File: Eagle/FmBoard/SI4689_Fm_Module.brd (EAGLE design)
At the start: 32.5 x 42.7 mm, 69 parts, among them IC1 TPS79318DBVR, IC2 SI4688-A10-GM, U1 TXS0104EPWR, U2 3.3V/150mA, X2 19.2MHz

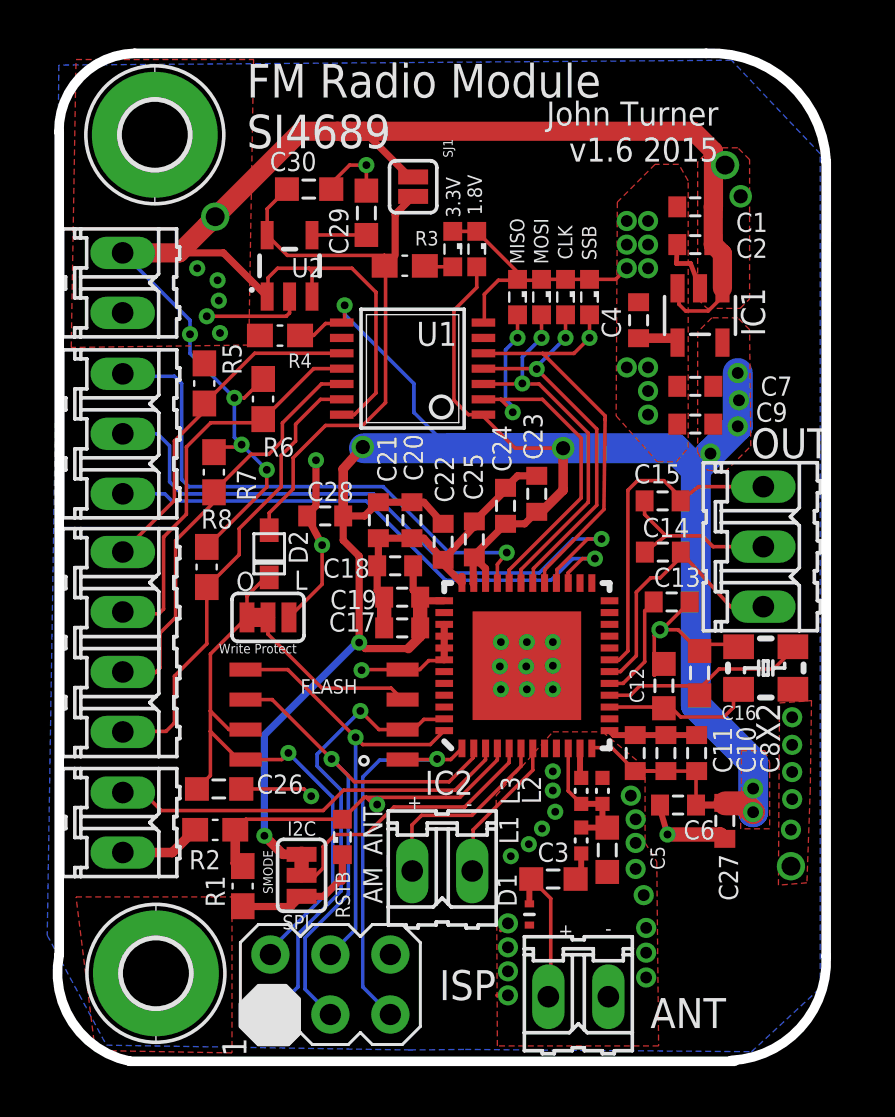
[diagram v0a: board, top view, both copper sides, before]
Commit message: Updated to the now working v1.7 of the radio module Made Radio Module arudino compatible so that it can be plugged directly into the arudino Moved to a S25FL132K0XMFI041 flash chip due to being cheaper and easier to program.
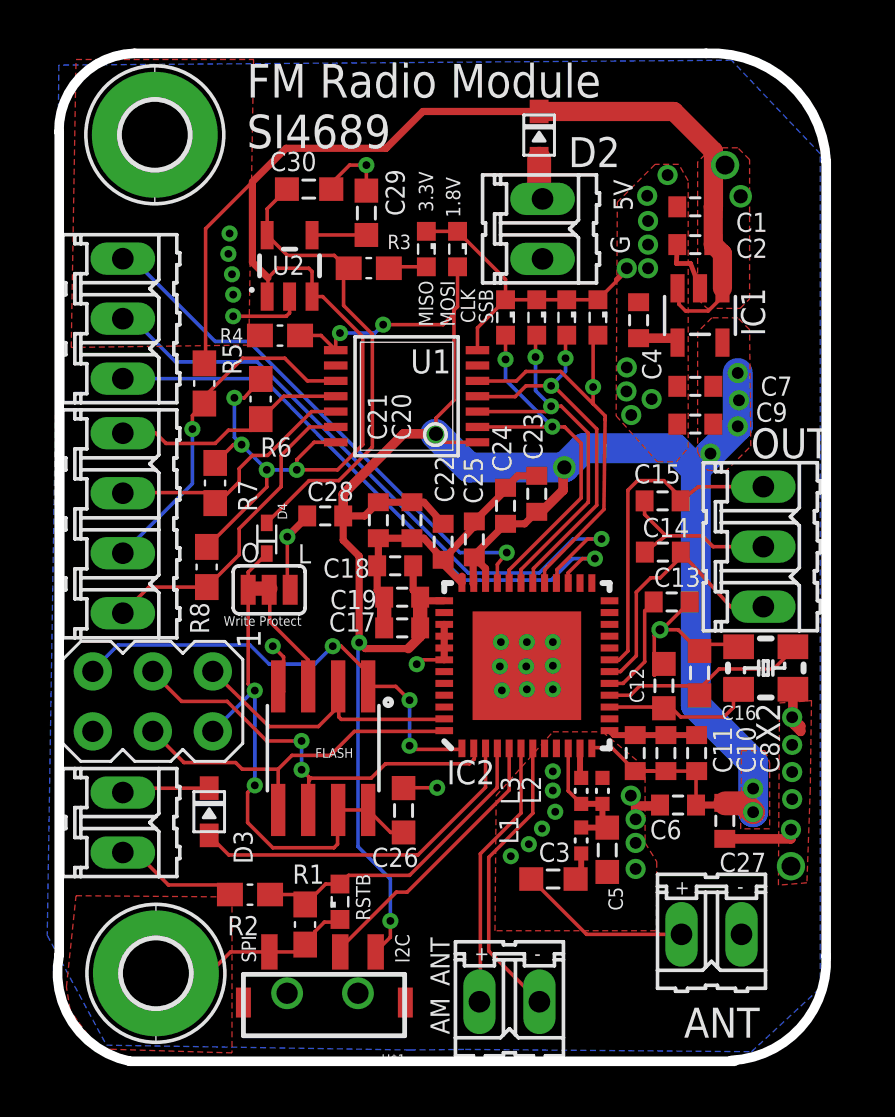
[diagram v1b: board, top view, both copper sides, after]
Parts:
- removed D1: ESD9L5.0, generisch:SOD923
- removed ISP: AVRISP-6, adafruit:AVRISP
- removed SJ1: SOLDERJUMPERNC, SparkFun-Retired:SJ_2S
- removed SMODE: (no value), SparkFun-Retired:SJ_3
- added D3: (no value), adafruit:SOD-323F
- added D4: (no value), SparkFun-DiscreteSemi:SOD523
- added ISP1: AVRISP-6, adafruit:AVRISP
- added U$1: SWITCH_SPDTMOUSER, SparkFun-Electromechanical:SSSS810701
- FLASH: value SST25VF016BSOIC -> SPI_FLASH-X25XXSMD; device john:SOIC8 -> SparkFun-DigitalIC:SO08
- IC2: value SI4688-A10-GM -> SI4689GM; device SI4688-A10-GM:QFN48 -> john:QFN48
- moved D2 21.1 mm to (20.6, 38.6), turned to 90 degrees
- moved POWER 17.9 mm to (20.5, 34.6)
- moved C26 7.88 mm to (14.9, 9.96), turned to 90 degrees
- moved ANT 6.23 mm to (27.9, 4.97)
- moved AM_ANT 6.23 mm to (19.4, 2.11)
- moved CONTROL 5.03 mm to (2.74, 22.1)
- moved DIGITALAUDIO 4.88 mm to (2.74, 30.8)
- moved R2 3.11 mm to (8.38, 6.40)
- moved R1 3.10 mm to (10.7, 5.13)
- moved RSTB 2.75 mm to (12.2, 6.10)
- moved FLASH 1.61 mm to (11.5, 12.6), turned to 180 degrees
- moved R3 1.53 mm to (13.4, 32.9)
- moved U1 1.20 mm to (15.0, 27.5)
- moved WP 1.17 mm to (9.19, 19.3)
- moved 3.3V 1.12 mm to (15.8, 33.7)
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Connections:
- removed net SPI0_CE0_N: CONTROL.1, R5.1, U1.10
- new net N$10: CHIP.1, D3.C
- new net N$19: D2.A, POWER.1
- new net SPI0_SSB: CONTROL.3, R5.1, U1.10
- net +1V8: now also U$1.S; no longer SMODE.3
- net 3.3V: now also D4.A; no longer D2.A, SJ1.2
- net FLASH_CE: now also ISP1.5; no longer ISP.5
- net FLASH_SCK: now also ISP1.3; no longer ISP.3
- net FLASH_SI: now also ISP1.4; no longer ISP.4
- net FLASH_SO: now also ISP1.1; no longer ISP.1
- net FLASH_VIN: now also D4.C, ISP1.2; no longer D2.C, ISP.2
- net GND: now also ISP1.6, U$1.O; no longer D1.A, ISP.6, SMODE.1
- net INT: now also D3.A; no longer CHIP.1
- net LDO_IN: now also D2.C; no longer POWER.1, SJ1.1
- net N$17: now also U$1.P; no longer SMODE.2
- net RF_IN: no longer D1.K
- net SPI0_MOSI: now also CONTROL.2; no longer CONTROL.3
- net SPI0_SCLK: now also CONTROL.1; no longer CONTROL.2
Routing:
- net SPI0_SSB: track 0.00 -> 14.7 mm, vias 0 -> 1
- net SPI0_CE0_N: track 14.4 -> 0.00 mm
- net +1V8: track 113.6 -> 105.4 mm, vias 11 -> 12
- net SPI0_SCLK: track 17.1 -> 10.1 mm
- net FLASH_SO: track 19.5 -> 13.3 mm, vias 1 -> 0
- net SPI0_MOSI: track 18.3 -> 12.1 mm
- net N$15: track 6.25 -> 12.4 mm
- net SPI0_MISO: track 19.5 -> 13.7 mm
- net FLASH_SCK: track 24.3 -> 18.5 mm, vias 1 -> 2
- net 3.3V: track 25.5 -> 20.4 mm
- net LDO_IN: track 77.4 -> 72.7 mm, vias 7 -> 6
- net FLASH_SI: track 19.6 -> 15.4 mm, vias 1 -> 0
- net FLASH_CE: track 16.8 -> 20.1 mm, vias 1 -> 3
- net N$16: track 8.36 -> 11.5 mm
- net N$10: track 0.66 -> 3.73 mm
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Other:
- board text added: "John Turner v1.7 2016"
- board text removed: "John Turner v1.6 2015"
